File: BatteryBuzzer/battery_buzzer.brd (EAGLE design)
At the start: 100 x 80 mm, 27 parts, among them Q1 IRFML8244, Q2 IRFML8244, Q3 P-CHANNEL-MOSFETSOT23-3, Q4 P-CHANNEL-MOSFETSOT23-3, Q5 P-CHANNEL-MOSFETSOT23-3

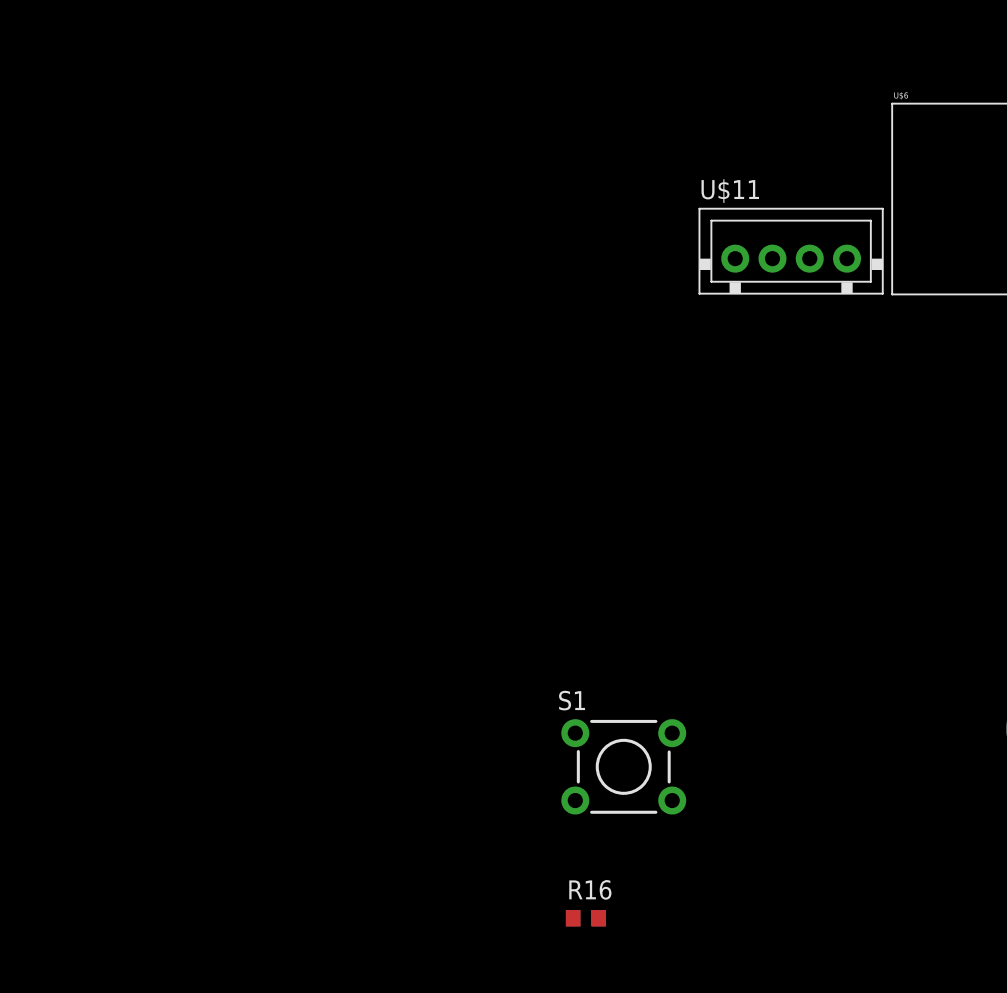
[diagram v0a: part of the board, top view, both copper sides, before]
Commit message: added DPST switch to libary, added power bypass to buzzer
power bypass so that with the push of a button the buzzer can turn out
powered by the battery alone.
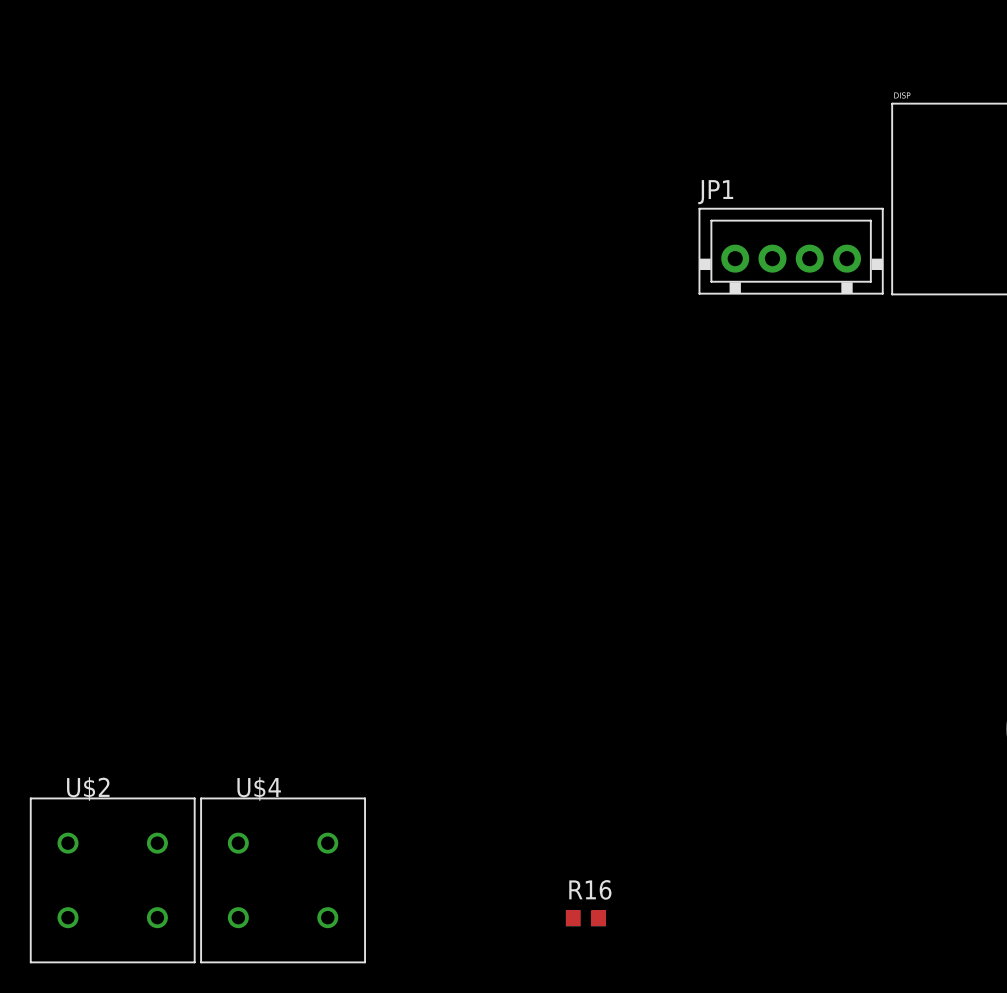
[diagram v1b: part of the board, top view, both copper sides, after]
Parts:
- removed S1: (no value), pie:TACTILE-PTH
- added U$2, U$4: DPST_SWITCH, pie:C&K_SWITCH
- renumbered U$11 to JP1, U$5 to UC1, U$6 to DISP
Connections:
- new net BGND: JP1.1, U$2.P2
- new net RAW: U$2.P1', UC1.RAW
- net 5V: now also U$4.P1, U$4.P2; no longer S1.1, S1.2
- net BCELL3: now also U$2.P1
- net C: no longer DISP.13
- net CALIB: now also U$4.P1', U$4.P2'; no longer S1.3, S1.4
- net GND: now also U$2.P2'

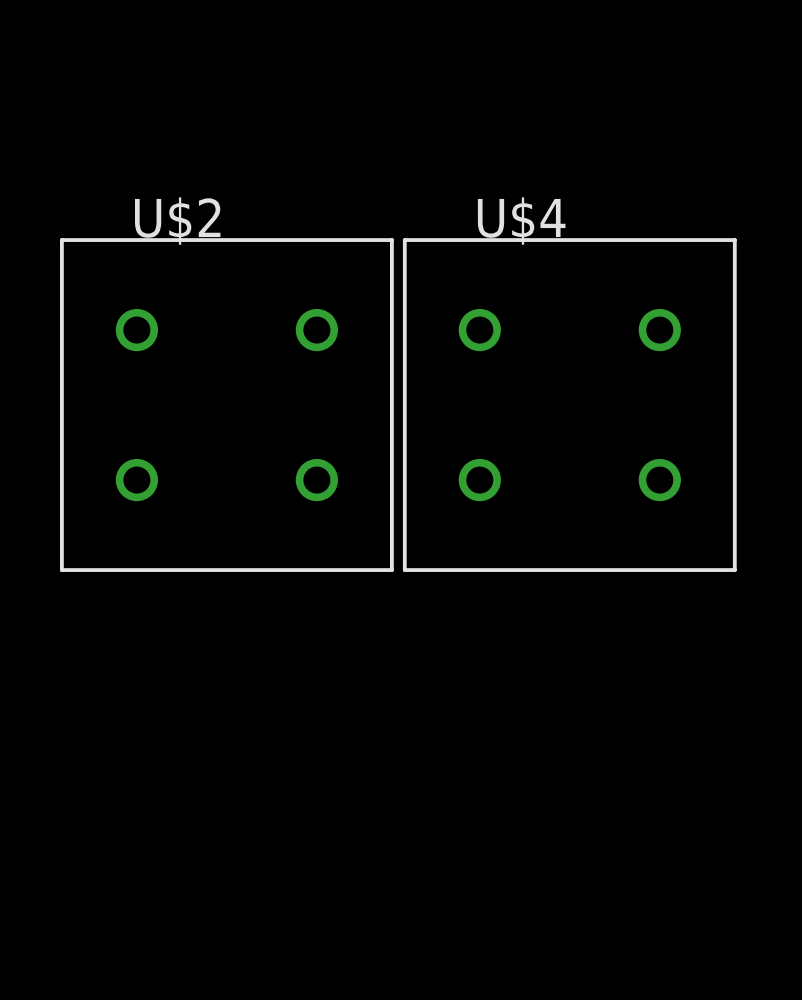
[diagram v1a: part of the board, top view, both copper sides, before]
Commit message: final additions to the battery buzzer schematic
cleaned things up, added the obligatory debug features.
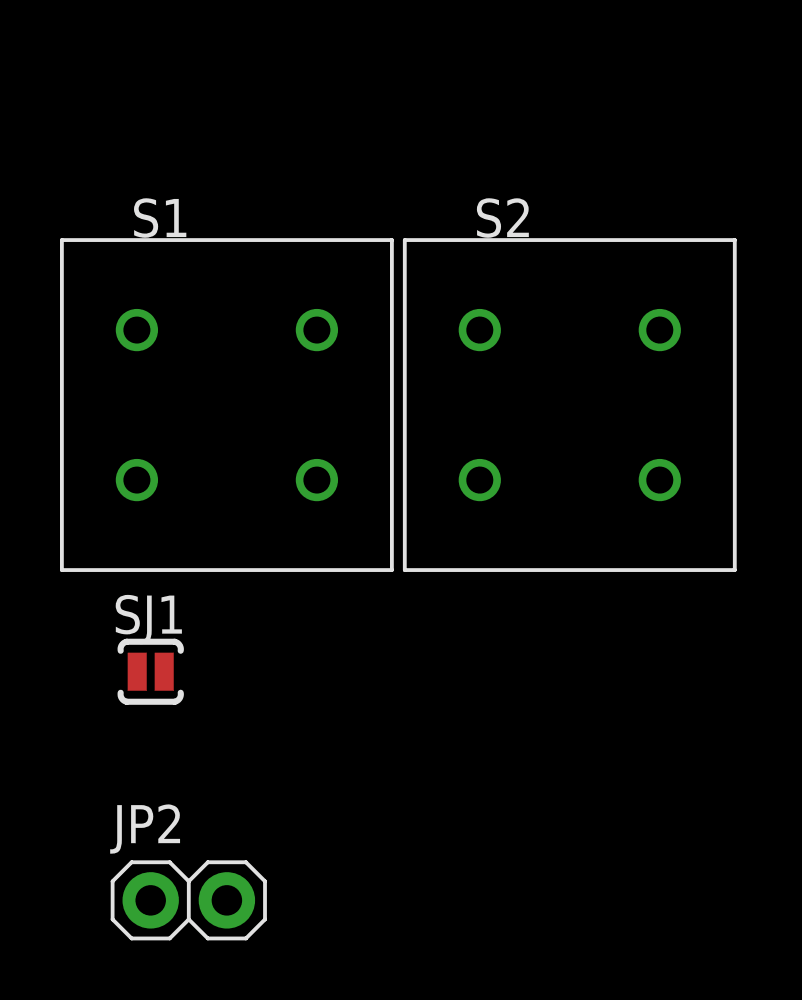
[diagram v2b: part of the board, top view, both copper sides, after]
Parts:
- added JP2: (no value), pie:1X02
- added SJ1: SOLDERJUMPERNO, pie:SJ_2S-NO
- renumbered U$2 to S1, U$4 to S2
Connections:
- net BGND: now also SJ1.1
- net GND: now also JP2.1, JP2.2, SJ1.2
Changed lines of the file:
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@@
 <attribute name="PIE-INT-REF-NUM" value="RESISTOR-GENERIC" x="-73.66" y="-3.81" size="1.778" layer="27" display="off"/>
 </element>
-<element name="U$4" library="pie" package="C&amp;K_SWITCH" value="DPST_SWITCH" x="-93.98" y="-1.27"/>
-<element name="U$2" library="pie" package="C&amp;K_SWITCH" value="DPST_SWITCH" x="-105.41" y="-1.27"/>
+<element name="S2" library="pie" package="C&amp;K_SWITCH" value="DPST_SWITCH" x="-93.98" y="-1.27"/>
+<element name="S1" library="pie" package="C&amp;K_SWITCH" value="DPST_SWITCH" x="-105.41" y="-1.27"/>
+<element name="SJ1" library="pie" package="SJ_2S-NO" value="SOLDERJUMPERNO" x="-107.95" y="-10.16">
+<attribute name="PIE-INT-REF-NUM" value="DNL" x="-107.95" y="-10.16" size="1.778" layer="27" display="off"/>
+</element>
+<element name="JP2" library="pie" package="1X02" value="" x="-106.68" y="-17.78">
+<attribute name="PIE-INT-REF-NUM" value="BULK-STOCK" x="-106.68" y="-17.78" size="1.778" layer="27" display="off"/>
+</element>
 </elements>
 <signals>
@@
 <contactref element="LS1" pad="A"/>
 <contactref element="UC1" pad="VCC"/>
-<contactref element="U$4" pad="P2"/>
-<contactref element="U$4" pad="P1"/>
+<contactref element="S2" pad="P2"/>
+<contactref element="S2" pad="P1"/>
 <wire x1="-96.98" y1="1.23" x2="-96.98" y2="-3.77" width="0" layer="19" extent="1-1"/>
 <wire x1="-39.37" y1="12.14000625" x2="-96.98" y2="1.23" width="0" layer="19" extent="1-1"/>
@@
 <contactref element="UC1" pad="GND@2"/>
 <contactref element="R16" pad="2"/>
-<contactref element="U$2" pad="P2'"/>
+<contactref element="S1" pad="P2'"/>
+<contactref element="JP2" pad="1"/>
+<contactref element="JP2" pad="2"/>
+<contactref element="SJ1" pad="2"/>
+<wire x1="-105.41" y1="-17.78" x2="-107.95" y2="-17.78" width="0" layer="19" extent="1-1"/>
+<wire x1="-107.5" y1="-10.16" x2="-107.95" y2="-17.78" width="0" layer="19" extent="1-1"/>
+<wire x1="-102.41" y1="-3.77" x2="-107.5" y2="-10.16" width="0" layer="19" extent="1-1"/>
 <wire x1="-72.81" y1="-3.81" x2="-102.41" y2="-3.77" width="0" layer="19" extent="1-1"/>
 <wire x1="-30.48" y1="22.86" x2="-72.81" y2="-3.81" width="0" layer="19" extent="1-1"/>
@@
 <contactref element="R1" pad="2"/>
 <contactref element="Q5" pad="2"/>
-<contactref element="U$2" pad="P1"/>
+<contactref element="S1" pad="P1"/>
 <wire x1="-56.13999375" y1="40.450009375" x2="-108.41" y2="1.23" width="0" layer="19" extent="1-1"/>
 <wire x1="-38.42" y1="70.12" x2="-56.13999375" y2="40.450009375" width="0" layer="19" extent="1-1"/>
@@
 <signal name="CALIB">
 <contactref element="UC1" pad="TXO"/>
-<contactref element="U$4" pad="P2'"/>
-<contactref element="U$4" pad="P1'"/>
+<contactref element="S2" pad="P2'"/>
+<contactref element="S2" pad="P1'"/>
 <contactref element="R16" pad="1"/>
 <wire x1="-90.98" y1="1.23" x2="-90.98" y2="-3.77" width="0" layer="19" extent="1-1"/>
@@
 <signal name="BGND">
 <contactref element="JP1" pad="1"/>
-<contactref element="U$2" pad="P2"/>
+<contactref element="S1" pad="P2"/>
+<contactref element="SJ1" pad="1"/>
+<wire x1="-108.41" y1="-3.77" x2="-108.4" y2="-10.16" width="0" layer="19" extent="1-1"/>
 <wire x1="-63.64000625" y1="40.450009375" x2="-108.41" y2="-3.77" width="0" layer="19" extent="1-1"/>
 </signal>
 <signal name="RAW">
 <contactref element="UC1" pad="RAW"/>
-<contactref element="U$2" pad="P1'"/>
+<contactref element="S1" pad="P1'"/>
 <wire x1="-15.24" y1="30.48" x2="-102.41" y2="1.23" width="0" layer="19" extent="1-1"/>
 </signal>

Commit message: some more pinremapping
to make routing easier... but routing starting now.
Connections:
- net CALIB: now also UC1.A3; no longer UC1.TXO
- net DP: now also UC1.TXO; no longer UC1.A3
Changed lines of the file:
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@@
 <signal name="DP">
 <contactref element="DISP" pad="7"/>
-<contactref element="UC1" pad="A3"/>
-<wire x1="-15.24" y1="20.32" x2="-26.67" y2="39.37" width="0" layer="19" extent="1-1"/>
+<contactref element="UC1" pad="TXO"/>
+<wire x1="-30.48" y1="30.48" x2="-26.67" y2="39.37" width="0" layer="19" extent="1-1"/>
 </signal>
 <signal name="F">
@@
 </signal>
 <signal name="CALIB">
-<contactref element="UC1" pad="TXO"/>
 <contactref element="S2" pad="P2'"/>
 <contactref element="S2" pad="P1'"/>
 <contactref element="R16" pad="1"/>
+<contactref element="UC1" pad="A3"/>
 <wire x1="-90.98" y1="1.23" x2="-90.98" y2="-3.77" width="0" layer="19" extent="1-1"/>
 <wire x1="-74.51" y1="-3.81" x2="-90.98" y2="-3.77" width="0" layer="19" extent="1-1"/>
-<wire x1="-30.48" y1="30.48" x2="-74.51" y2="-3.81" width="0" layer="19" extent="1-1"/>
+<wire x1="-15.24" y1="20.32" x2="-74.51" y2="-3.81" width="0" layer="19" extent="1-1"/>
 </signal>
 <signal name="BGND">

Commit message: initial layout.
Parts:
- moved SJ1 165.4 mm to (56.4, 8.38), turned to 270 degrees
- moved S1 154.1 mm to (48.5, 6.35), turned to 180 degrees
- moved JP2 145.3 mm to (37.1, 3.56)
- moved Q2 124.6 mm to (48.8, 14.5)
- moved R6 124.2 mm to (43.4, 13.5), turned to 180 degrees
- moved JP1 122.8 mm to (61.2, 19.3), turned to 90 degrees
- moved S2 122.2 mm to (27.9, 6.35)
- moved R5 117.1 mm to (43.2, 18.3)
- moved R4 115.0 mm to (48.8, 23.4)
- moved R3 111.9 mm to (48.8, 20.8)
- moved R16 111.5 mm to (37.1, 8.89)
- moved R2 109.0 mm to (48.8, 18.3)
- moved Q5 104.3 mm to (54.1, 24.9)
- moved R1 103.8 mm to (54.1, 28.7)
- moved Q4 102.8 mm to (54.1, 20.8)
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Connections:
- net BUZZER_SIGNAL: now also UC1.RXI; no longer UC1.3
- net DIG_1: now also UC1.3; no longer UC1.RXI
- net DIV_EN: now also UC1.TXO; no longer UC1.2
- net DP: now also UC1.2; no longer UC1.TXO
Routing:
- added copper zone on layer 16, net 5V
- added copper zone on layer 1, net GND
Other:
- board size 100 x 80 mm -> 69.8 x 50.8 mm

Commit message: route partially done.
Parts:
- moved R5 1.78 mm to (45.0, 18.3)
- moved R7 1.78 mm to (45.0, 20.8)
- moved R8 1.78 mm to (45.0, 23.4)
- moved JP2 1.02 mm to (38.1, 3.56)
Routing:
- net RAW: track 0.00 -> 42.1 mm
- net BCELL3: track 0.00 -> 38.4 mm
- net N$1: track 0.00 -> 23.6 mm
- net IO2: track 0.00 -> 14.6 mm
- net BGND: track 0.00 -> 13.5 mm
- net IO0: track 0.00 -> 13.0 mm
- net IO1: track 0.00 -> 12.8 mm
- net N$5: track 0.00 -> 10.7 mm
- net CALIB: track 0.00 -> 10.3 mm
- net BCELL1: track 0.00 -> 7.22 mm
- net N$6: track 0.00 -> 6.91 mm
- net BCELL2: track 0.00 -> 6.57 mm
- net DIV_EN: track 0.00 -> 6.20 mm
- net N$7: track 0.00 -> 5.95 mm
- net N$4: track 0.00 -> 5.57 mm
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
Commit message: switched some pin assignments
to make routing easier.
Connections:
- net BUZZER_SIGNAL: now also UC1.A3; no longer UC1.RXI
- net CALIB: now also UC1.10; no longer UC1.A3
- net D: now also UC1.RXI; no longer UC1.10
- net DIV_EN: now also UC1.16; no longer UC1.TXO
- net E: now also UC1.TXO; no longer UC1.16
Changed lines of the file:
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@@
 <contactref element="R9" pad="1"/>
 <contactref element="R11" pad="2"/>
-<contactref element="UC1" pad="RXI"/>
 <wire x1="47.41" y1="36.576" x2="44.03" y2="36.576" width="0.254" layer="1"/>
 <wire x1="44.03" y1="36.576" x2="43.942" y2="36.664" width="0.254" layer="1"/>
-<wire x1="23.622" y1="39.624" x2="43.942" y2="36.664" width="0" layer="19" extent="1-1"/>
+<contactref element="UC1" pad="A3"/>
+<wire x1="38.862" y1="32.004" x2="44.03" y2="36.576" width="0" layer="19" extent="1-1"/>
 </signal>
 <signal name="N$1">
@@
 <contactref element="Q2" pad="1"/>
 <contactref element="R6" pad="2"/>
-<contactref element="UC1" pad="TXO"/>
 <wire x1="47.818" y1="13.478" x2="46.8724" y2="13.478" width="0.254" layer="1"/>
 <wire x1="46.8724" y1="13.478" x2="45.72" y2="14.6304" width="0.254" layer="1"/>
 <wire x1="45.72" y1="14.6304" x2="43.7524" y2="14.6304" width="0.254" layer="1"/>
 <wire x1="43.7524" y1="14.6304" x2="42.584" y2="13.462" width="0.254" layer="1"/>
-<wire x1="43.7524" y1="14.6304" x2="23.622" y2="42.164" width="0" layer="19" extent="1-1"/>
+<contactref element="UC1" pad="16"/>
+<wire x1="38.862" y1="16.764" x2="42.584" y2="13.462" width="0" layer="19" extent="1-1"/>
 </signal>
 <signal name="N$2">
@@
 <signal name="D">
 <contactref element="DISP" pad="3"/>
-<contactref element="UC1" pad="10"/>
-<wire x1="12.446" y1="17.018" x2="38.862" y2="14.224" width="0" layer="19" extent="1-1"/>
+<contactref element="UC1" pad="RXI"/>
+<wire x1="12.446" y1="17.018" x2="23.622" y2="39.624" width="0" layer="19" extent="1-1"/>
 </signal>
 <signal name="E">
 <contactref element="DISP" pad="5"/>
-<contactref element="UC1" pad="16"/>
-<wire x1="12.446" y1="22.098" x2="38.862" y2="16.764" width="0" layer="19" extent="1-1"/>
+<contactref element="UC1" pad="TXO"/>
+<wire x1="12.446" y1="22.098" x2="23.622" y2="42.164" width="0" layer="19" extent="1-1"/>
 </signal>
 <signal name="DP">
@@
 <contactref element="S2" pad="P1'"/>
 <contactref element="R16" pad="1"/>
-<contactref element="UC1" pad="A3"/>
 <wire x1="30.94" y1="3.85" x2="30.94" y2="8.85" width="0.254" layer="1"/>
 <wire x1="30.94" y1="8.85" x2="36.194" y2="8.85" width="0.254" layer="1"/>
 <wire x1="36.194" y1="8.85" x2="36.234" y2="8.89" width="0.254" layer="1"/>
-<wire x1="36.234" y1="8.89" x2="38.862" y2="32.004" width="0" layer="19" extent="1-1"/>
+<contactref element="UC1" pad="10"/>
+<wire x1="36.234" y1="8.89" x2="38.862" y2="14.224" width="0" layer="19" extent="1-1"/>
 </signal>
 <signal name="BGND">

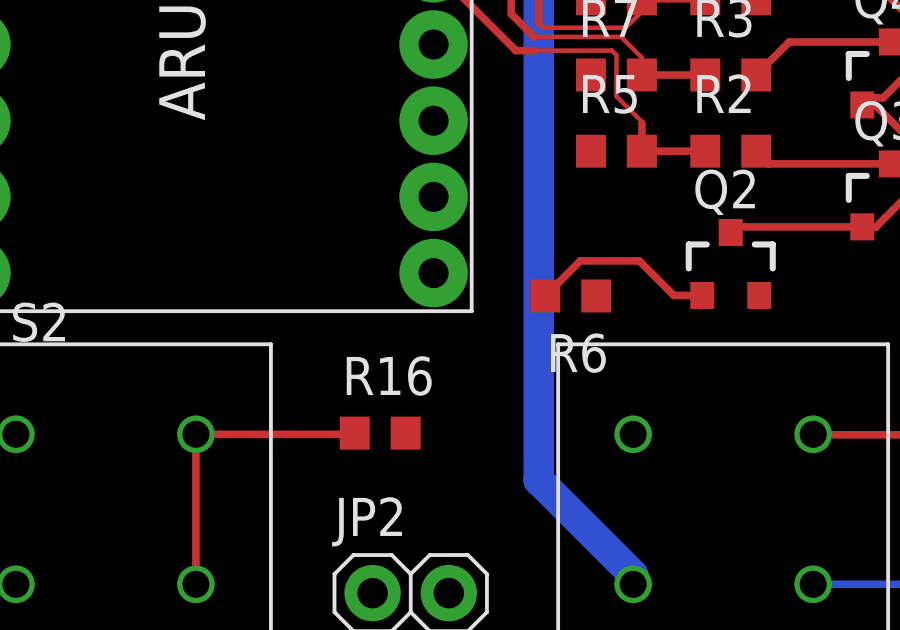
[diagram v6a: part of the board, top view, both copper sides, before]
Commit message: more pin remapping.
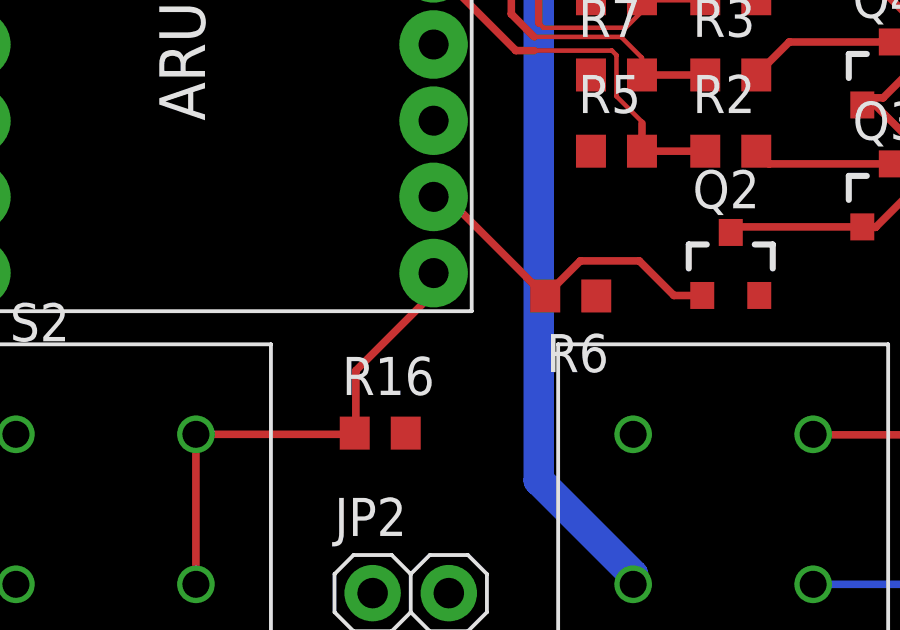
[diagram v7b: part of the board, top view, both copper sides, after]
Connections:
- net DIG_1: now also UC1.6; no longer UC1.3
- net DIG_2: now also UC1.5; no longer UC1.4
- net DIG_3: now also UC1.4; no longer UC1.5
- net DIG_4: now also UC1.3; no longer UC1.6
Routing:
- net CALIB: track 10.3 -> 16.7 mm
- net DIV_EN: track 6.20 -> 11.3 mm
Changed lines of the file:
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@@
 <wire x1="43.7524" y1="14.6304" x2="42.584" y2="13.462" width="0.254" layer="1"/>
 <contactref element="UC1" pad="16"/>
-<wire x1="38.862" y1="16.764" x2="42.584" y2="13.462" width="0" layer="19" extent="1-1"/>
+<wire x1="38.862" y1="16.764" x2="39.282" y2="16.764" width="0.254" layer="1"/>
+<wire x1="39.282" y1="16.764" x2="42.584" y2="13.462" width="0.254" layer="1"/>
 </signal>
 <signal name="N$2">
@@
 <signal name="DIG_1">
 <contactref element="R14" pad="2"/>
-<contactref element="UC1" pad="3"/>
-<wire x1="18.122" y1="11.938" x2="23.622" y2="29.464" width="0" layer="19" extent="1-1"/>
+<contactref element="UC1" pad="6"/>
+<wire x1="18.122" y1="11.938" x2="23.622" y2="21.844" width="0" layer="19" extent="1-1"/>
 </signal>
 <signal name="D">
@@
 <signal name="DIG_2">
 <contactref element="R12" pad="2"/>
-<contactref element="UC1" pad="4"/>
-<wire x1="18.122" y1="14.478" x2="23.622" y2="26.924" width="0" layer="19" extent="1-1"/>
+<contactref element="UC1" pad="5"/>
+<wire x1="18.122" y1="14.478" x2="23.622" y2="24.384" width="0" layer="19" extent="1-1"/>
 </signal>
 <signal name="DIG_3">
 <contactref element="R13" pad="2"/>
-<contactref element="UC1" pad="5"/>
-<wire x1="18.122" y1="24.638" x2="23.622" y2="24.384" width="0" layer="19" extent="1-1"/>
+<contactref element="UC1" pad="4"/>
+<wire x1="18.122" y1="24.638" x2="23.622" y2="26.924" width="0" layer="19" extent="1-1"/>
 </signal>
 <signal name="DIG_4">
 <contactref element="R17" pad="2"/>
-<contactref element="UC1" pad="6"/>
-<wire x1="23.622" y1="21.844" x2="18.122" y2="29.718" width="0" layer="19" extent="1-1"/>
+<contactref element="UC1" pad="3"/>
+<wire x1="18.122" y1="29.718" x2="23.622" y2="29.464" width="0" layer="19" extent="1-1"/>
 </signal>
 <signal name="CALIB">
@@
 <wire x1="36.194" y1="8.85" x2="36.234" y2="8.89" width="0.254" layer="1"/>
 <contactref element="UC1" pad="10"/>
-<wire x1="36.234" y1="8.89" x2="38.862" y2="14.224" width="0" layer="19" extent="1-1"/>
+<wire x1="38.862" y1="14.224" x2="38.862" y2="13.5636" width="0.254" layer="1"/>
+<wire x1="38.862" y1="13.5636" x2="36.2712" y2="10.9728" width="0.254" layer="1"/>
+<wire x1="36.2712" y1="10.9728" x2="36.2712" y2="8.9272" width="0.254" layer="1"/>
+<wire x1="36.2712" y1="8.9272" x2="36.234" y2="8.89" width="0.254" layer="1"/>
 </signal>
 <signal name="BGND">
